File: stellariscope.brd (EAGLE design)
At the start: 60.5 x 60.5 mm, 37 parts, among them U1 74238, U10 74AHC1G126DBV, U2 74238, U3 TLC5947PWP, U4 TLC59213, U5 741G79DCT, U6 74AHC1G126DBV, U7 74AHC1G126DBV, U8 74AHC1G32DBV, U9 74AHC1G32DBV

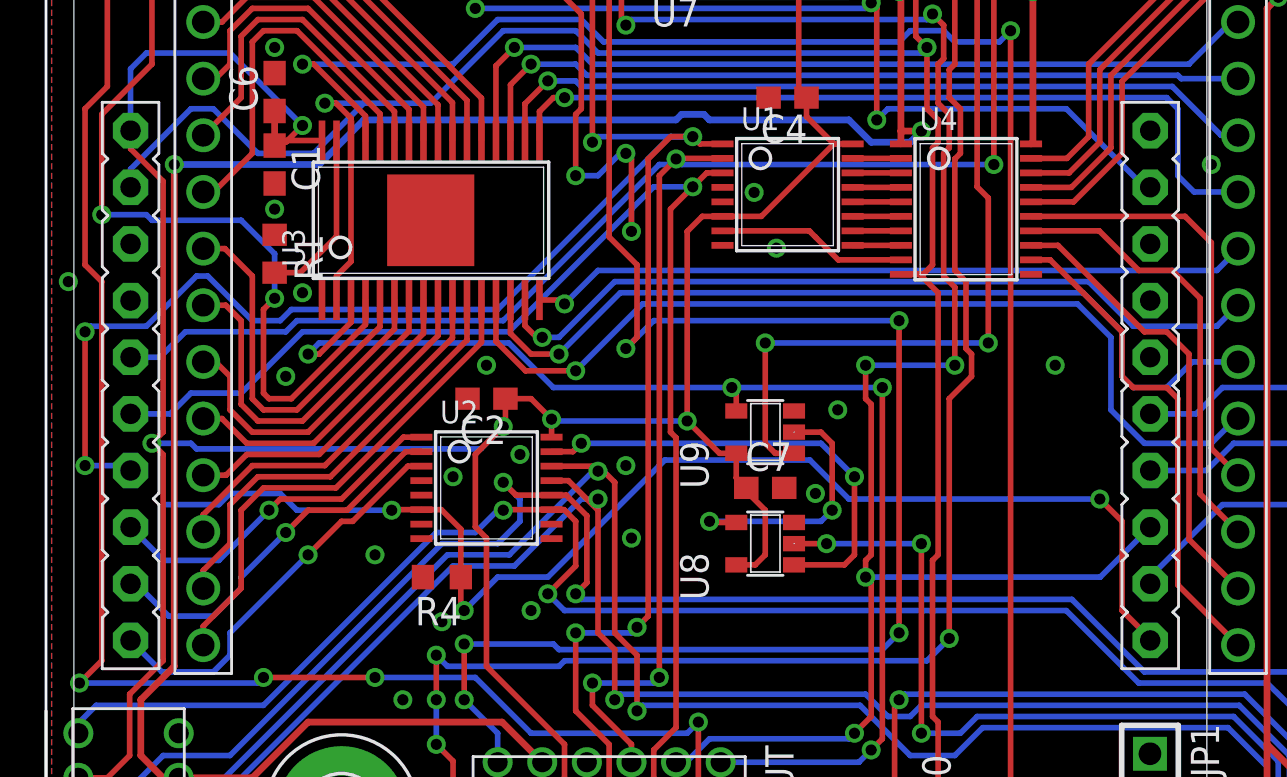
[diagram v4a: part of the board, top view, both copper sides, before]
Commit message: Fixed the serial issue right this time, miscellaneous test code changes (not done)
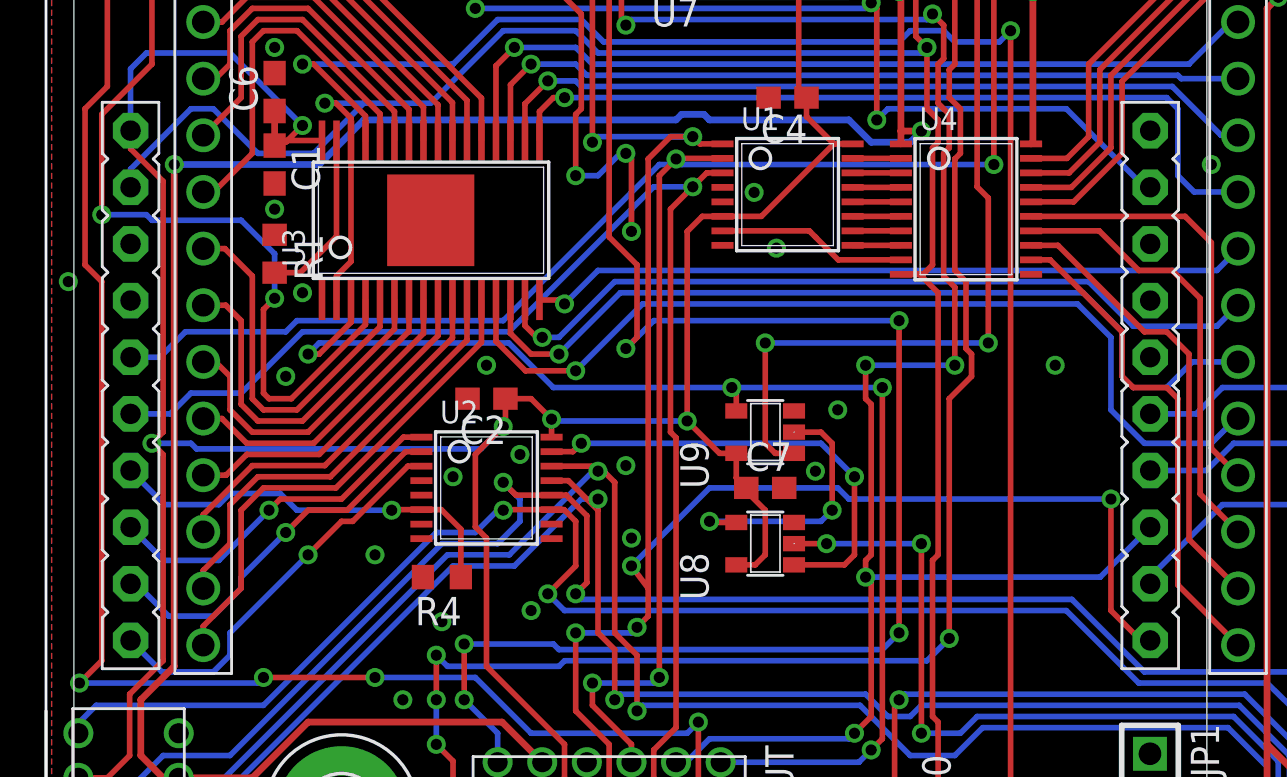
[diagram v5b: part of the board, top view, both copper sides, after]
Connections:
- net N$29: now also LAUNCHPAD.P1.5; no longer LAUNCHPAD.P2.3
- net N$36: now also LAUNCHPAD.P2.3; no longer LAUNCHPAD.P1.5
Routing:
- net N$29: track 57.2 -> 18.5 mm, vias 3 -> 1
- net N$36: track 178.9 -> 171.0 mm
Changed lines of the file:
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@@
 <via x="0.75" y="27.25" extent="1-16" drill="0.5"/>
 <via x="19.5" y="23.5" extent="1-16" drill="0.5"/>
-<via x="34.25" y="17.75" extent="1-16" drill="0.5"/>
+<via x="34.25" y="18.75" extent="1-16" drill="0.5"/>
 <via x="11.25" y="26.75" extent="1-16" drill="0.5"/>
 <via x="24.5" y="48.75" extent="1-16" drill="0.5"/>
@@
 <wire x1="18.35" y1="16.15" x2="17.475" y2="17.025" width="0.254" layer="1"/>
 <wire x1="16.5822" y1="17.025" x2="17.475" y2="17.025" width="0.254" layer="1"/>
-<contactref element="LAUNCHPAD" pad="P2.3"/>
-<wire x1="49.26" y1="11.16" x2="49.26" y2="11.24" width="0.254" layer="1"/>
-<wire x1="49.26" y1="11.24" x2="48" y2="12.5" width="0.254" layer="1"/>
-<wire x1="48" y1="12.5" x2="48" y2="16.5" width="0.254" layer="1"/>
-<wire x1="48" y1="16.5" x2="47" y2="17.5" width="0.254" layer="1"/>
-<via x="47" y="17.5" extent="1-16" drill="0.5"/>
-<wire x1="47" y1="17.5" x2="35.75" y2="17.5" width="0.254" layer="16"/>
-<wire x1="35.75" y1="17.5" x2="34" y2="19.25" width="0.254" layer="16"/>
-<wire x1="34" y1="19.25" x2="27.5" y2="19.25" width="0.254" layer="16"/>
-<wire x1="27.5" y1="19.25" x2="22.25" y2="14" width="0.254" layer="16"/>
-<wire x1="22.25" y1="14" x2="20" y2="14" width="0.254" layer="16"/>
-<wire x1="20" y1="14" x2="18.5" y2="12.5" width="0.254" layer="16"/>
-<via x="18.5" y="12.5" extent="1-16" drill="0.5"/>
-<wire x1="18.35" y1="14" x2="18.35" y2="12.65" width="0.254" layer="1"/>
-<wire x1="18.35" y1="12.65" x2="18.5" y2="12.5" width="0.254" layer="1"/>
+<contactref element="LAUNCHPAD" pad="P1.5"/>
+<wire x1="5.07" y1="17.25" x2="3.54" y2="18.78" width="0.254" layer="16"/>
 </signal>
 <signal name="SIN">
@@
 <wire x1="51.5" y1="52.5" x2="50" y2="51" width="0.254" layer="16"/>
 <wire x1="50" y1="51" x2="40.25" y2="51" width="0.254" layer="16"/>
-<wire x1="6.5" y1="27.5" x2="7" y2="27.5" width="0.254" layer="16"/>
-<wire x1="7" y1="27.5" x2="9" y2="25.5" width="0.254" layer="16"/>
-<wire x1="9" y1="25.5" x2="10.25" y2="25.5" width="0.254" layer="16"/>
-<wire x1="10.25" y1="25.5" x2="10.75" y2="26" width="0.254" layer="16"/>
-<wire x1="10.75" y1="26" x2="20" y2="26" width="0.254" layer="16"/>
-<wire x1="20" y1="26" x2="27.75" y2="33.75" width="0.254" layer="16"/>
 <via x="28.75" y="33.75" extent="1-16" drill="0.5"/>
 <wire x1="28.75" y1="33.75" x2="29" y2="33.5" width="0.254" layer="1"/>
@@
 <via x="26.25" y="11.75" extent="1-16" drill="0.5"/>
 <wire x1="26.25" y1="11.75" x2="26.75" y2="12.25" width="0.254" layer="1"/>
-<wire x1="26.75" y1="12.25" x2="26.75" y2="32.75" width="0.254" layer="1"/>
+<wire x1="26.75" y1="12.25" x2="26.75" y2="13.5" width="0.254" layer="1"/>
+<wire x1="26.75" y1="13.5" x2="26.75" y2="32.75" width="0.254" layer="1"/>
 <wire x1="24.5" y1="33.75" x2="24.25" y2="33.5" width="0.254" layer="16"/>
 <via x="24.25" y="33.5" extent="1-16" drill="0.5"/>
@@
 <wire x1="20" y1="50.75" x2="20.25" y2="50.75" width="0.254" layer="16"/>
 <wire x1="20.25" y1="50.75" x2="20.5" y2="50.5" width="0.254" layer="16"/>
-<contactref element="LAUNCHPAD" pad="P1.5"/>
-<wire x1="6.5" y1="27.5" x2="4.25" y2="25.25" width="0.254" layer="16"/>
-<wire x1="4.25" y1="25.25" x2="1.75" y2="25.25" width="0.254" layer="16"/>
-<wire x1="1.75" y1="25.25" x2="1.5" y2="25" width="0.254" layer="16"/>
-<via x="1.5" y="25" extent="1-16" drill="0.5"/>
-<wire x1="1.5" y1="25" x2="1.5" y2="19" width="0.254" layer="1"/>
-<via x="1.5" y="19" extent="1-16" drill="0.5"/>
-<wire x1="1.5" y1="19" x2="3.32" y2="19" width="0.254" layer="16"/>
-<wire x1="3.32" y1="19" x2="3.54" y2="18.78" width="0.254" layer="16"/>
+<contactref element="LAUNCHPAD" pad="P2.3"/>
+<wire x1="49.26" y1="11.16" x2="48.84" y2="11.16" width="0.254" layer="1"/>
+<wire x1="48.84" y1="11.16" x2="47.5" y2="12.5" width="0.254" layer="1"/>
+<wire x1="47.5" y1="12.5" x2="47.5" y2="17.5" width="0.254" layer="1"/>
+<via x="47.5" y="17.5" extent="1-16" drill="0.5"/>
+<wire x1="47.5" y1="17.5" x2="35.75" y2="17.5" width="0.254" layer="16"/>
+<wire x1="35.75" y1="17.5" x2="35.25" y2="18" width="0.254" layer="16"/>
+<wire x1="35.25" y1="18" x2="29.5" y2="18" width="0.254" layer="16"/>
+<wire x1="29.5" y1="18" x2="26" y2="14.5" width="0.254" layer="16"/>
+<via x="26" y="14.5" extent="1-16" drill="0.5"/>
+<wire x1="26" y1="14.5" x2="26.75" y2="13.5" width="0.254" layer="1"/>
 </signal>
 <signal name="XLAT">

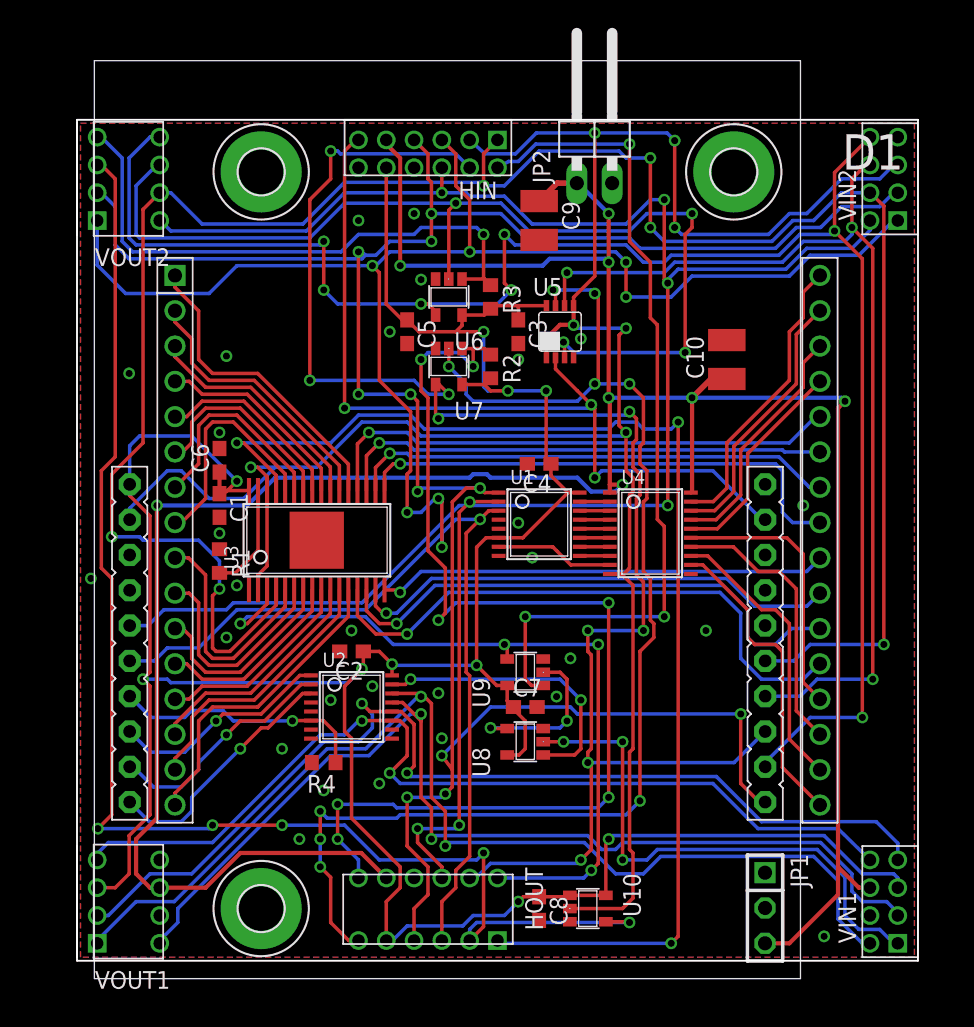
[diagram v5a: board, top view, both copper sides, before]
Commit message: -- added pull-downs to all inputs from the Launchpad -- added delay filters to counting lines so they work now.
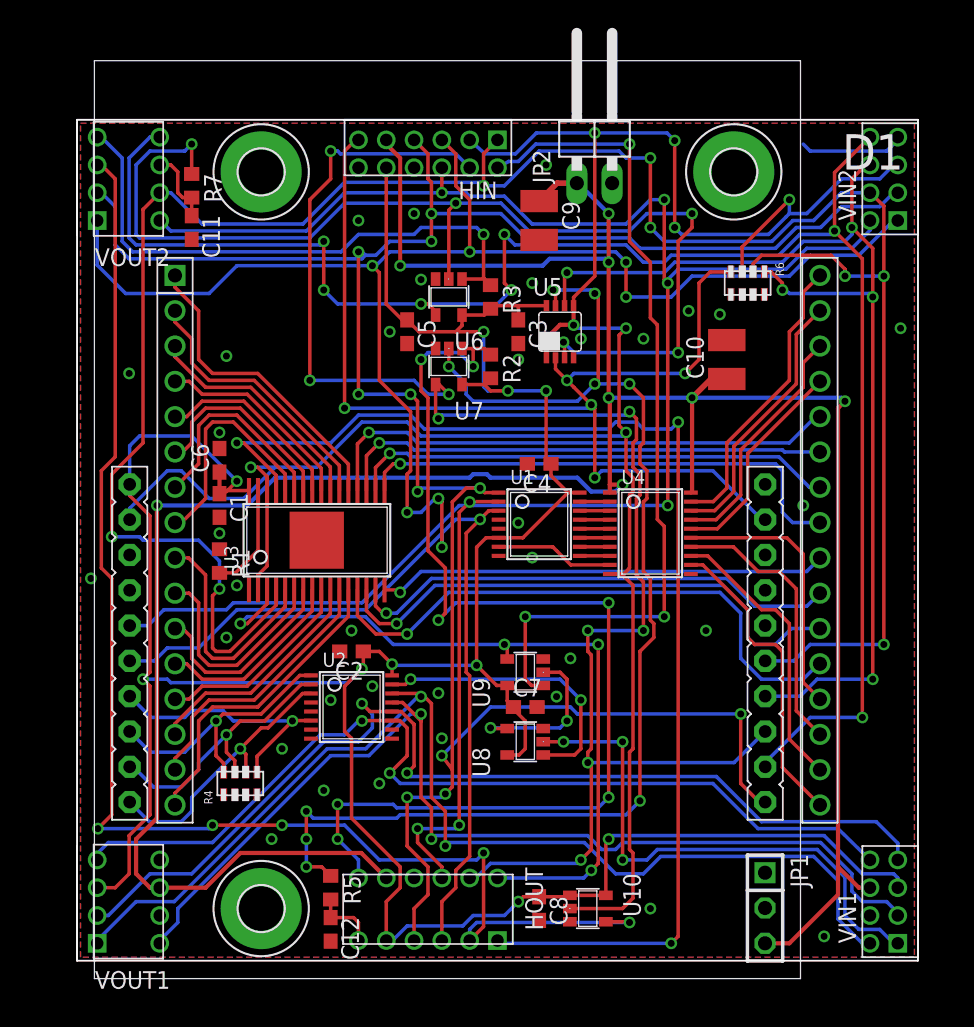
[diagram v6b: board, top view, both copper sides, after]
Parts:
- added C11, C12: 100n, resistor:C0603
- added R5, R7: 10K, resistor:R0603
- added R6: 10K, res-cap-arrays:CTS742C083-RES
- R4: device resistor:R0603 -> res-cap-arrays:CTS742C083-RES
- moved R4 6.18 mm to (11.5, 12.5), turned to 90 degrees
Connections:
- new net N$28: C12.1, HOUT.11, R5.2
- new net N$42: C11.1, R7.2, VOUT2.6
- net GND: now also C11.2, C12.2, R4.1, R4.3, R4.5, R4.7, R6.2, R6.4, R6.6, R6.8; no longer R4.2
- net HCNT_OUT: now also R5.1; no longer HOUT.11
- net N$29: now also R4.8; no longer R4.1
- net N$31: now also R4.2
- net N$32: now also R4.4
- net N$33: now also R4.6
- net N$37: now also R6.7
- net N$38: now also R6.1
- net SIN: now also R6.3
- net VCNT_OUT: now also R7.1; no longer VOUT2.6
- net XLAT: now also R6.5
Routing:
- net N$37: track 61.4 -> 79.7 mm, vias 3 -> 5
- net SIN: track 155.4 -> 166.6 mm, vias 6 -> 8
- net N$38: track 71.2 -> 80.0 mm, vias 3 -> 5
- net XLAT: track 164.7 -> 172.3 mm, vias 7 -> 8
- net GND: track 0.00 -> 7.54 mm, vias 29 -> 36
- net VCNT_OUT: track 74.4 -> 80.1 mm, vias 4 -> 5
- net N$42: track 0.00 -> 5.45 mm
- net N$28: track 0.00 -> 4.74 mm
- net N$31: track 15.9 -> 19.9 mm
- net HCNT_OUT: track 93.4 -> 89.6 mm
- net N$32: track 17.0 -> 19.9 mm
- net N$33: track 18.0 -> 19.9 mm
